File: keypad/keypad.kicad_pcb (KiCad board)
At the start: 2 copper layers, 78.6 x 111.1 mm, 59 parts, among them J1 AVR-ISP-6, SW1 num, SW10 #5, SW11 #6, SW12 plu1, SW13 #1, SW14 #2, SW15 #3, SW16 ent0, SW17 #0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

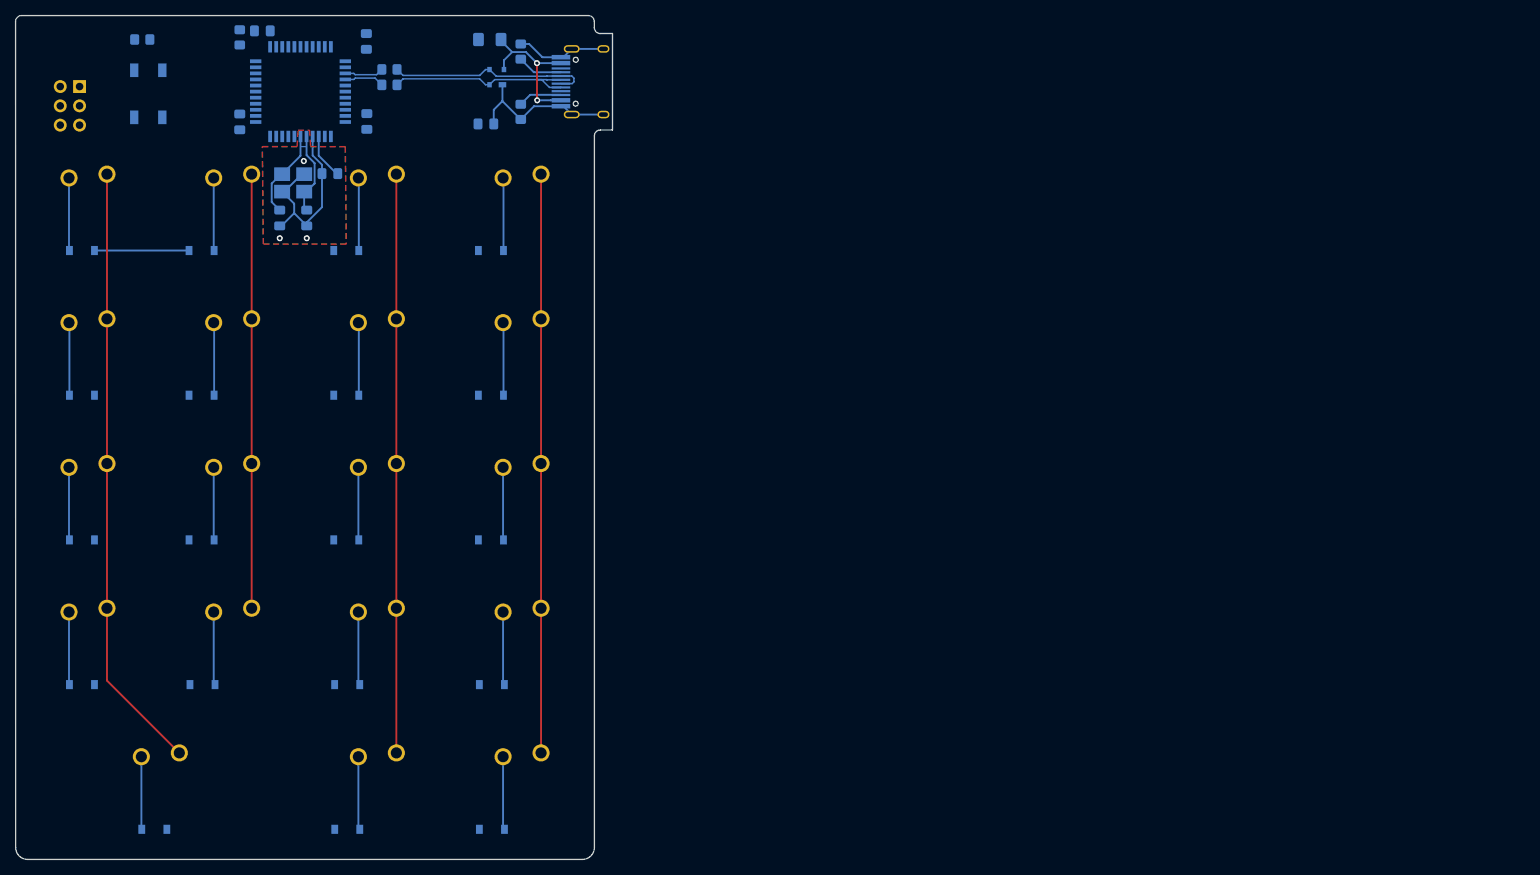
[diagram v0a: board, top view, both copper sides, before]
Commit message: Connected 5V/GND to USB
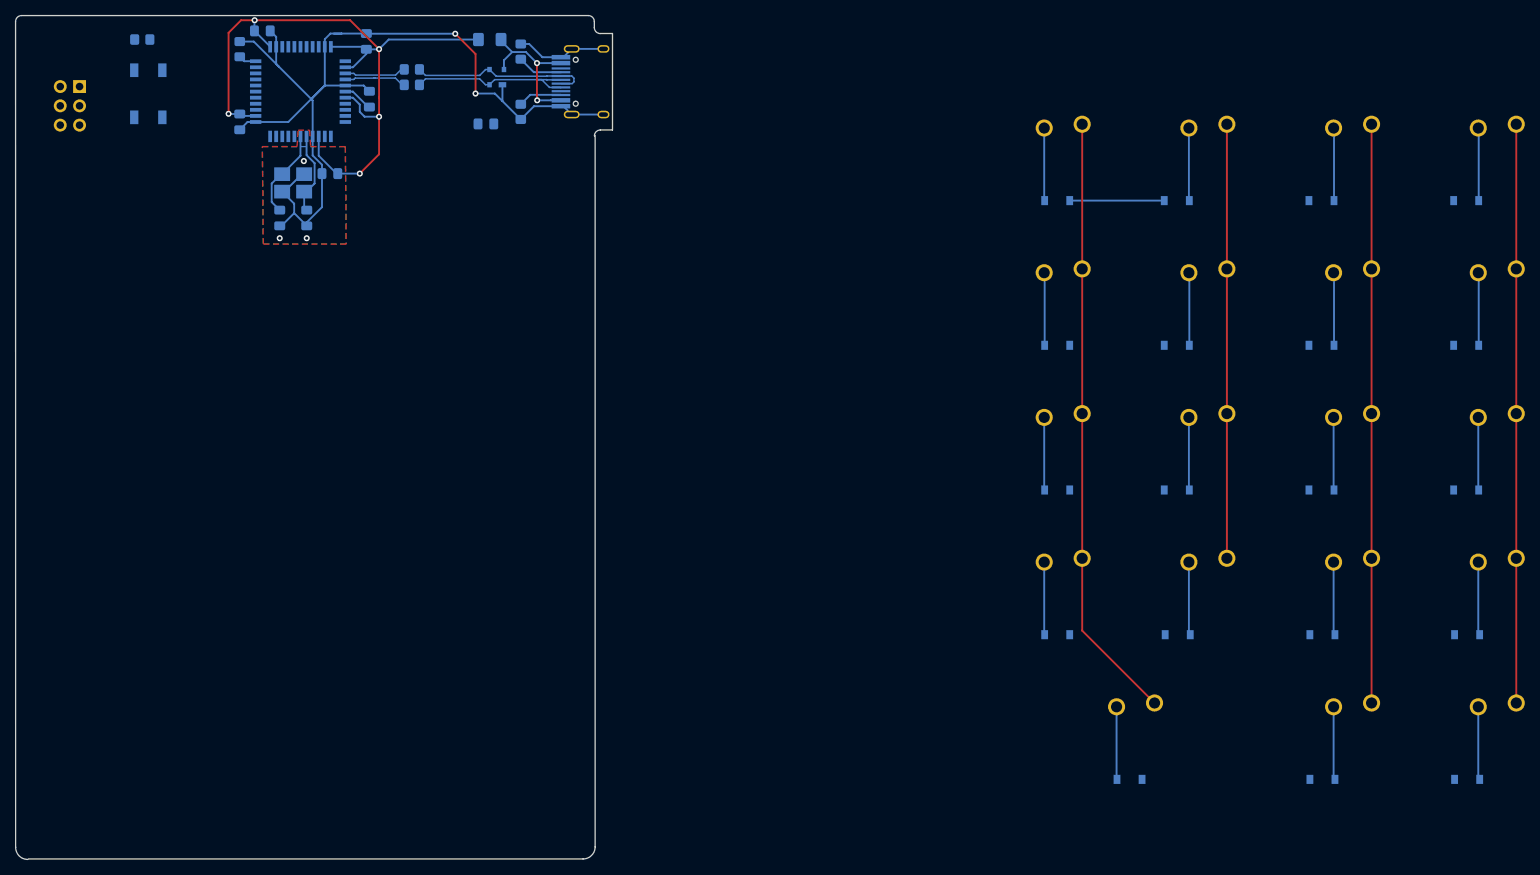
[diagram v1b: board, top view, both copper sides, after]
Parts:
- moved D14 128.6 mm to (188.7, 119.6)
- moved D17 128.6 mm to (182.4, 138.7)
- moved D1 128.6 mm to (172.8, 62.5)
- moved D10 128.6 mm to (188.6, 100.6)
- moved D11 128.6 mm to (207.6, 100.6)
- moved D12 128.6 mm to (226.7, 100.6)
- moved D13 128.6 mm to (172.8, 119.6)
- moved D15 128.6 mm to (207.8, 119.6)
- moved D16 128.6 mm to (226.8, 119.6)
- moved D18 128.6 mm to (207.8, 138.7)
- moved D19 128.6 mm to (226.8, 138.7)
- moved D2 128.6 mm to (188.6, 62.5)
- moved D3 128.6 mm to (207.6, 62.5)
- moved D4 128.6 mm to (226.7, 62.5)
- moved D5 128.6 mm to (172.8, 81.5)
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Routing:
- net +5V: track 6.02 -> 97.4 mm, vias 0 -> 5
- net GND: track 58.6 -> 138.0 mm, vias 3 -> 5
- net Net-(C8-Pad1): track 0.00 -> 4.02 mm
- net /D+: track 5.25 -> 8.32 mm
- net /D-: track 5.17 -> 8.16 mm
- net DP: track 26.1 -> 23.1 mm
- net DN: track 26.8 -> 23.8 mm
- net Net-(R4-Pad1): track 0.00 -> 2.34 mm
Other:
- outline, holes or cut-outs redrawn
